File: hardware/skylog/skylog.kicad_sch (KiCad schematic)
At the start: 5 parts, among them U1 ESP32-DevKitC, U2 Sensor_TempUmid_RS485_5V_24V, U3 KY-028, U4 GY-302_BH1750, U5 RS485_TTL_V2_OSHWLab

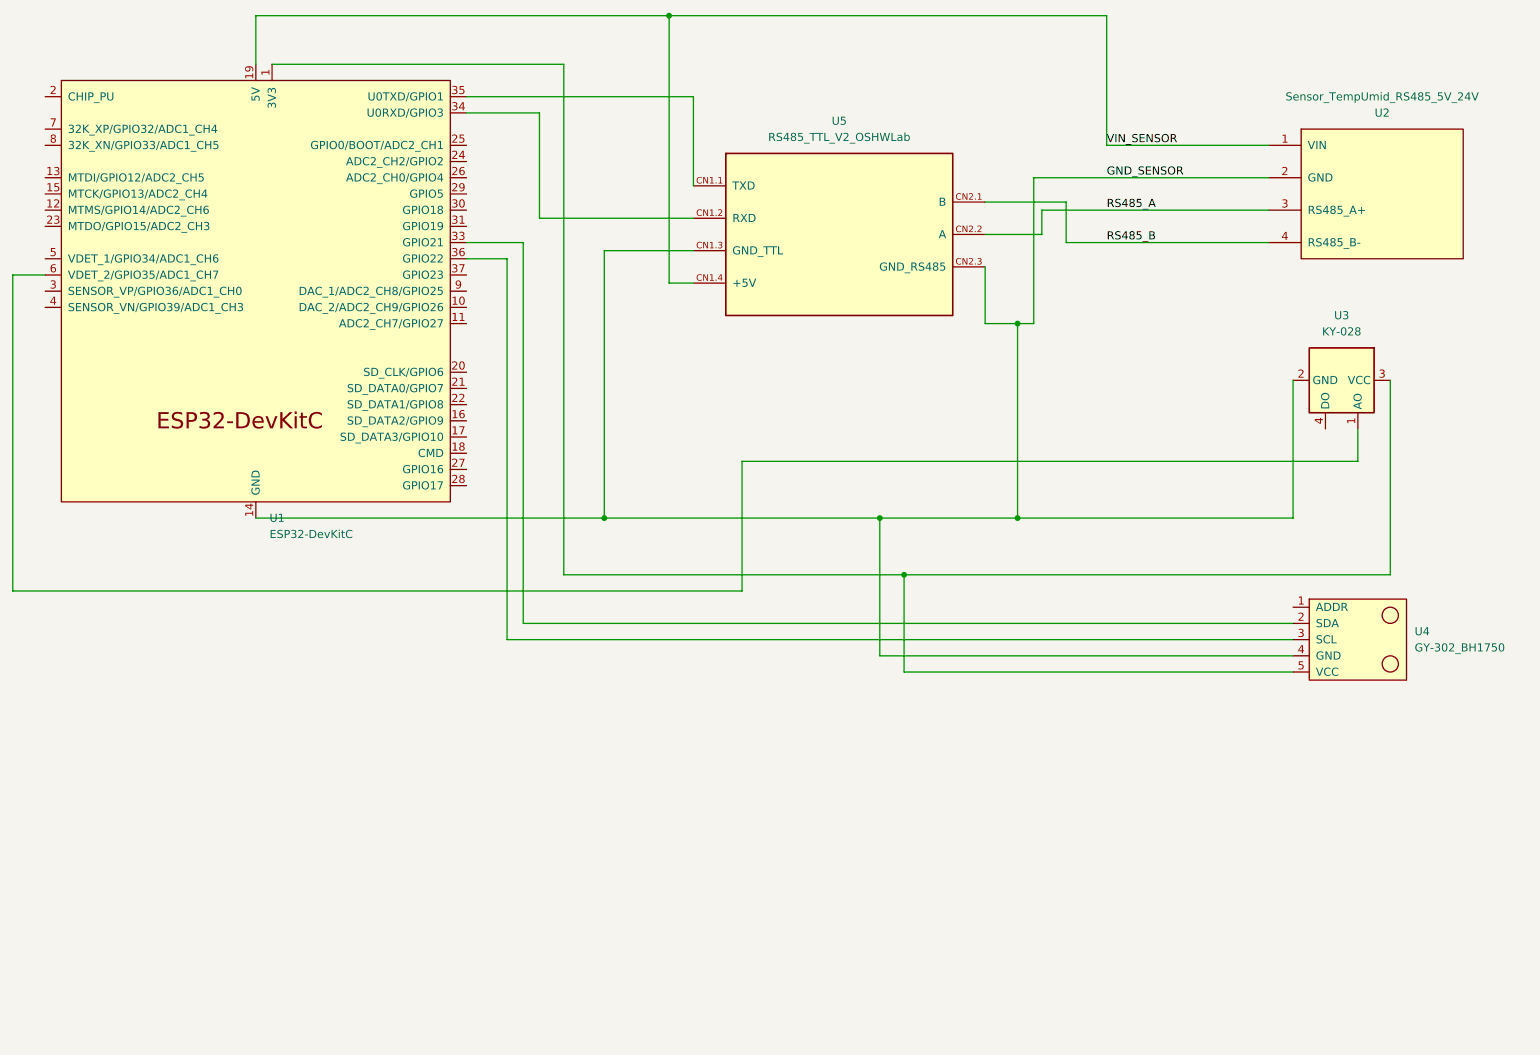
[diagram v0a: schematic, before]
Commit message: Add new footprints for wire jumpers and pads; update symbol library table
- Created a new footprint for a 10mm wire jumper (Wire_Jumper_P10.00mm) with specifications for soldered connections and pad dimensions.
- Added a footprint for a wire pad (Wire_Pad_D1.2mm) designed for insulated power wire connections, including pad and drill sizes.
- Updated the symbol library table to include additional libraries for Espressif components, sensor modules, and standard power symbols for KiCad 10.
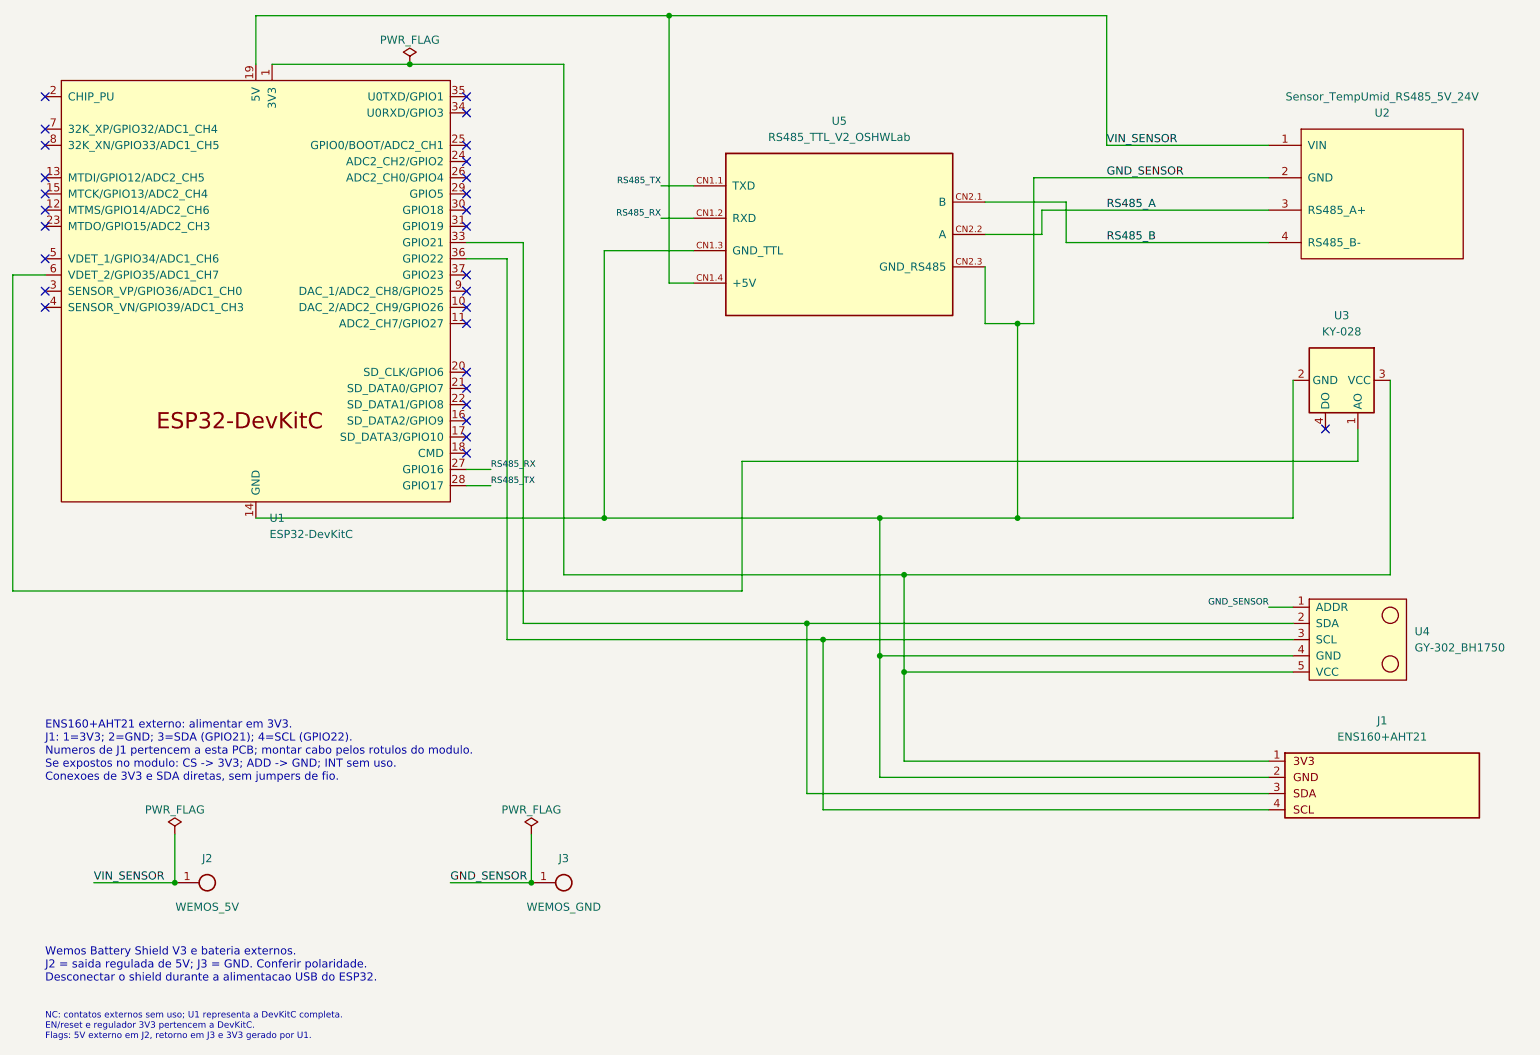
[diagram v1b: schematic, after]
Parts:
- added J1: ENS160+AHT21, skylog:ENS160_AHT21_1x04_P2.54mm, symbol skylog:ENS160_AHT21_Interface
- added J2: WEMOS_5V, skylog:Wire_Pad_D1.2mm, symbol skylog:Wire_Pad
- added J3: WEMOS_GND, skylog:Wire_Pad_D1.2mm, symbol skylog:Wire_Pad
- U1: footprint ESP32:ESP32-DevKitC -> skylog:ESP32-DevKitC_BoardEdge
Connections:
- net GND_SENSOR: now also U4.1 (ADDR), J1.2, J3.1
- net VIN_SENSOR: now also J2.1
- net at U1.1 (3V3), U3.3 (VCC), U4.5 (VCC): now also J1.1
- net at U1.35 (U0TXD/GPIO1): no longer U5.CN1.1 (TXD)
- net at U1.34 (U0RXD/GPIO3): no longer U5.CN1.2 (RXD)
- net RS485_RX: now reaches U1.27 (GPIO16)
- net RS485_RX: now also U5.CN1.2 (RXD)
- net RS485_TX: now reaches U1.28 (GPIO17)
- net RS485_TX: now also U5.CN1.1 (TXD)
- net at U1.33 (GPIO21), U4.2 (SDA): now also J1.3
- net at U1.36 (GPIO22), U4.3 (SCL): now also J1.4
- no-connect marks 0 -> 29
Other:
- note added: "ENS160+AHT21 externo: alimentar em 3V3. J1: 1=3V3; 2=GND; 3=SDA (GPIO21); 4=SCL (GPIO22). Numeros de J1 pertencem a esta PCB; montar cabo pelos rotulos do modulo. Se expostos no modulo: CS -> 3V3; ADD -> GND; INT sem uso. Conexoes de 3V3 e SDA diretas, sem jumpers de fio."
- note added: "NC: contatos externos sem uso; U1 representa a DevKitC completa. EN/reset e regulador 3V3 pertencem a DevKitC. Flags: 5V externo em J2, retorno em J3 e 3V3 gerado por U1."
- note added: "Wemos Battery Shield V3 e bateria externos. J2 = saida regulada de 5V; J3 = GND. Conferir polaridade. Desconectar o shield durante a alimentacao USB do ESP32."
